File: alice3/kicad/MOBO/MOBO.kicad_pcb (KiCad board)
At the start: 2 copper layers, 74.9 x 114.3 mm, 40 parts, among them CON1 SD_Card, P1 CONN_01X05, P2 CONN_01X01, SW1 RESET, SW2 SOFT RESET, U2 VGA_daughter_board, U3 Propeller_P8X32A-D40, U4 24LC256, U5 Propeller_Plug, U6 MiniM4-D40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

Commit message: Fix PCB v1 issues we identified Feb 6 2016
Route GND and 3V3
Swap labels for Y1 and U1
Move large IC labels so they'll be visible after soldering sockets
Rotate SD card header 180 degrees
Move RAM decoupling cap closer to RAM
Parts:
- moved C5 64.0 mm to (103.0, 77.7), turned to 0 degrees
- moved CON1 22.6 mm to (50.8, 130.6), turned to 180 degrees
- moved R13 15.4 mm to (94.2, 139.4)
- moved R2 12.7 mm to (53.3, 61.0), turned to 180 degrees
- moved R16 9.72 mm to (105.9, 140.0), turned to 90 degrees
- moved R15 8.99 mm to (103.1, 140.0), turned to 90 degrees
- moved R14 8.48 mm to (94.2, 136.9)
- moved R11 8.22 mm to (94.2, 144.5)
- moved R12 8.22 mm to (94.2, 142.0)
- moved R7 7.62 mm to (53.3, 53.3)
- moved C1 7.06 mm to (85.3, 141.0)
- moved U2 5.59 mm to (104.1, 116.1)
- moved P1 4.06 mm to (104.1, 120.9)
- moved R6 2.54 mm to (53.3, 50.8)
- moved R5 2.54 mm to (53.3, 48.3)
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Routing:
- net GND: track 0.00 -> 551.6 mm
- net +3V3: track 65.1 -> 436.7 mm
- net D5: track 191.6 -> 147.3 mm, vias 1 -> 0
- net D7: track 182.3 -> 140.4 mm, vias 0 -> 2
- net A14: track 107.5 -> 68.3 mm, vias 2 -> 1
- net Net-(P1-Pad3): track 78.7 -> 116.0 mm, vias 0 -> 1
- net /IORQ: track 163.0 -> 126.3 mm, vias 0 -> 1
- net /IO/DI: track 85.6 -> 114.3 mm, vias 2 -> 1
- net /IO/CS: track 64.3 -> 89.5 mm, vias 0 -> 1
- net /IO/SCK: track 64.2 -> 89.1 mm, vias 1 -> 0
- net /RESET: track 95.7 -> 120.5 mm, vias 1 -> 0
- net /IO/DO: track 114.2 -> 89.7 mm
- net +5V: track 73.4 -> 52.3 mm, vias 4 -> 2
- net A2: track 91.2 -> 111.7 mm
- net D3: track 160.0 -> 141.3 mm, vias 5 -> 3
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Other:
- net class Default: clearance 0.2 -> 0.156; trace_width 0.25 -> 0.156
- rule trace_clearance: 0.2 -> 0.156
- rule trace_min: 0.2 -> 0.156
- board text added: "Alice 3 Z80/Propeller/ARM v2 lawrence.kesteloot@gmail.com grantham@plunk.org http://plunk.org/alice3"
- board text added: "Alice 3 v2 2016 BG & LK"
- board text removed: "Alice 3 Z80/Propeller/ARM v1 lawrence.kesteloot@gmail.com grantham@plunk.org lkesteloot.github.io/alice/alice3/"
- board text removed: "Alice 3 v1 2016 BG & LK"

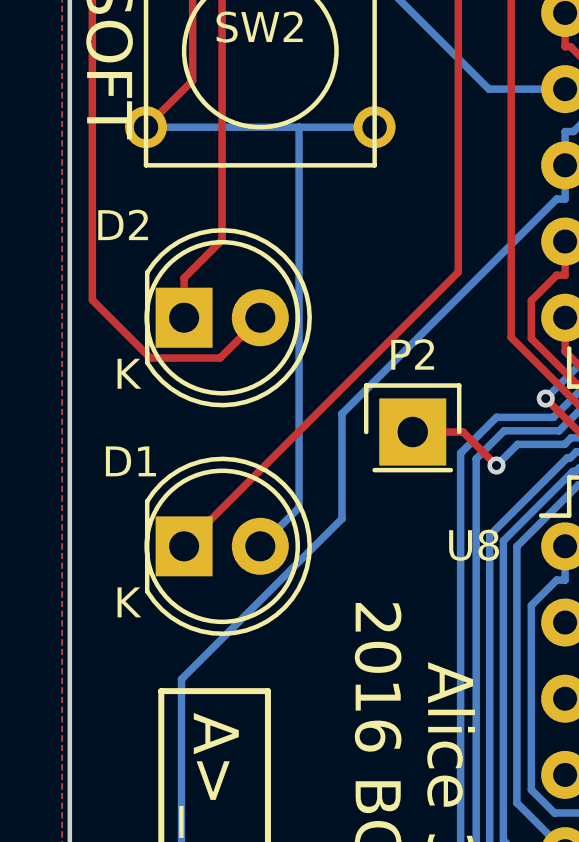
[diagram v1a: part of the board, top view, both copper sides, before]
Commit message: Add PWR and DBG silk screen for LEDS
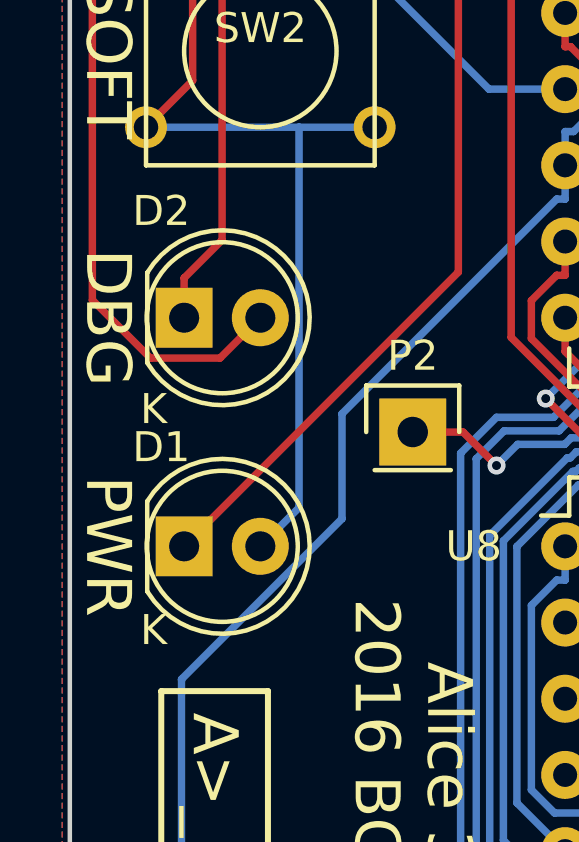
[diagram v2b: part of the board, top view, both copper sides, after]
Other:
- board text added: "DBG"
- board text added: "PWR"
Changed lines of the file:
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@@
     (links 179)
     (no_connects 0)
-    (area 45.644999 32.944999 120.725001 149.206143)
+    (area 45.466 32.766 120.904001 149.162143)
     (thickness 1.6)
-    (drawings 15)
+    (drawings 17)
     (tracks 1288)
     (zones 0)
@@
     (descr "LED 5mm round vertical")
     (tags "LED 5mm round vertical")
-    (fp_text reference D1 (at -1.778 -2.794) (layer F.SilkS)
+    (fp_text reference D1 (at -0.762 -3.302) (layer F.SilkS)
       (effects (font (size 1 1) (thickness 0.15)))
     )
@@
     (fp_line (start -1.23 1.5) (end -1.23 -1.5) (layer F.SilkS) (width 0.15))
     (fp_circle (center 1.27 0) (end 0.97 -2.5) (layer F.SilkS) (width 0.15))
-    (fp_text user K (at -1.905 1.905) (layer F.SilkS)
+    (fp_text user K (at -1.016 2.794) (layer F.SilkS)
       (effects (font (size 1 1) (thickness 0.15)))
     )
@@
     (descr "LED 5mm round vertical")
     (tags "LED 5mm round vertical")
-    (fp_text reference D2 (at -2.032 -3.048) (layer F.SilkS)
+    (fp_text reference D2 (at -0.762 -3.556) (layer F.SilkS)
       (effects (font (size 1 1) (thickness 0.15)))
     )
@@
     (fp_line (start -1.23 1.5) (end -1.23 -1.5) (layer F.SilkS) (width 0.15))
     (fp_circle (center 1.27 0) (end 0.97 -2.5) (layer F.SilkS) (width 0.15))
-    (fp_text user K (at -1.905 1.905) (layer F.SilkS)
+    (fp_text user K (at -1.016 3.048) (layer F.SilkS)
       (effects (font (size 1 1) (thickness 0.15)))
     )
@@
     )
   )
+  (gr_text PWR (at 46.99 93.98 270) (layer F.SilkS)
+    (effects (font (size 1.5 1.5) (thickness 0.3)))
+  )
+  (gr_text DBG (at 46.99 86.36 270) (layer F.SilkS)
+    (effects (font (size 1.5 1.5) (thickness 0.3)))
+  )
   (gr_text BARTCONN (at 107.188 125.984 90) (layer F.SilkS)
